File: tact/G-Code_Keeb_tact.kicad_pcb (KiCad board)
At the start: 2 copper layers, 116 x 62 mm, 28 parts, among them SW1 X+100, SW10 Y-1, SW11 Y-10, SW12 Y-100, SW13 Z+10, SW14 Z+1, SW15 Z+0.1, SW16 Z-0.1, SW17 Z-1, SW18 Z-10, SW19 HOME, SW2 X+10, SW20 HOME X, SW21 HOME Y, SW22 HOME XY, SW23 HOME Z, SW3 locked, SW5 X-10, SW6 X-100, SW7 Y+100, SW8 Y+10, SW9 Y+1, U1 Pico

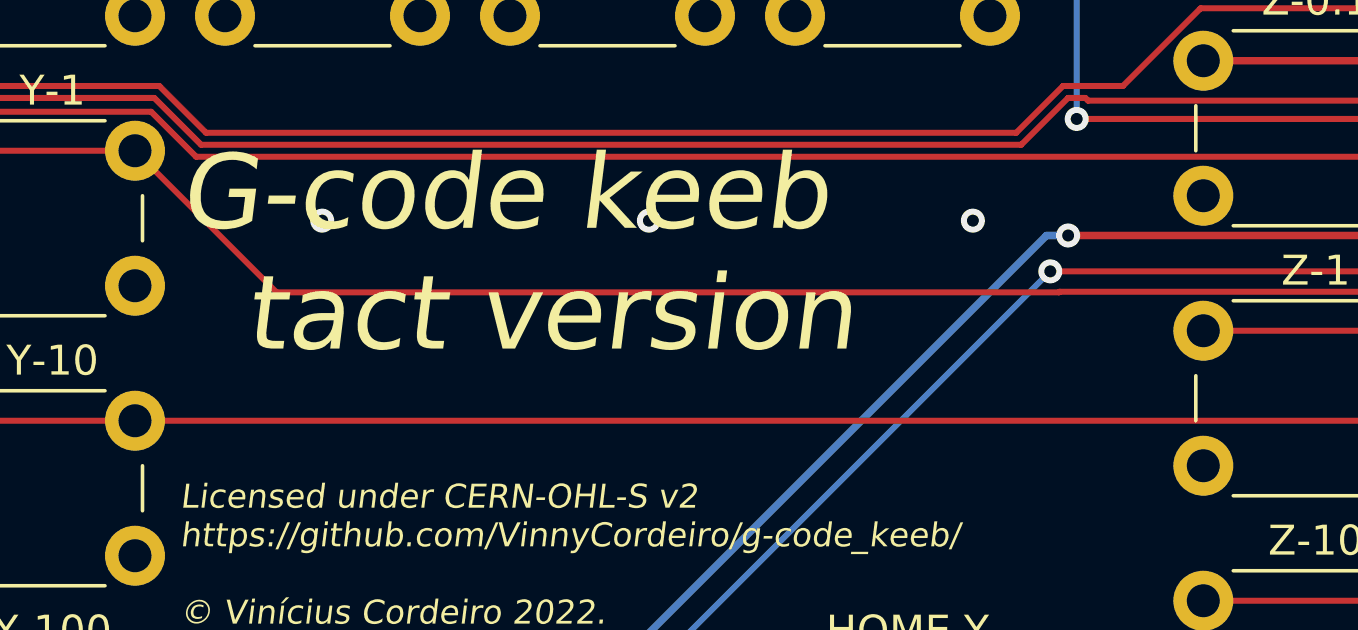
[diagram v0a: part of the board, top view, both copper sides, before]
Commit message: Adjusting silkscreen
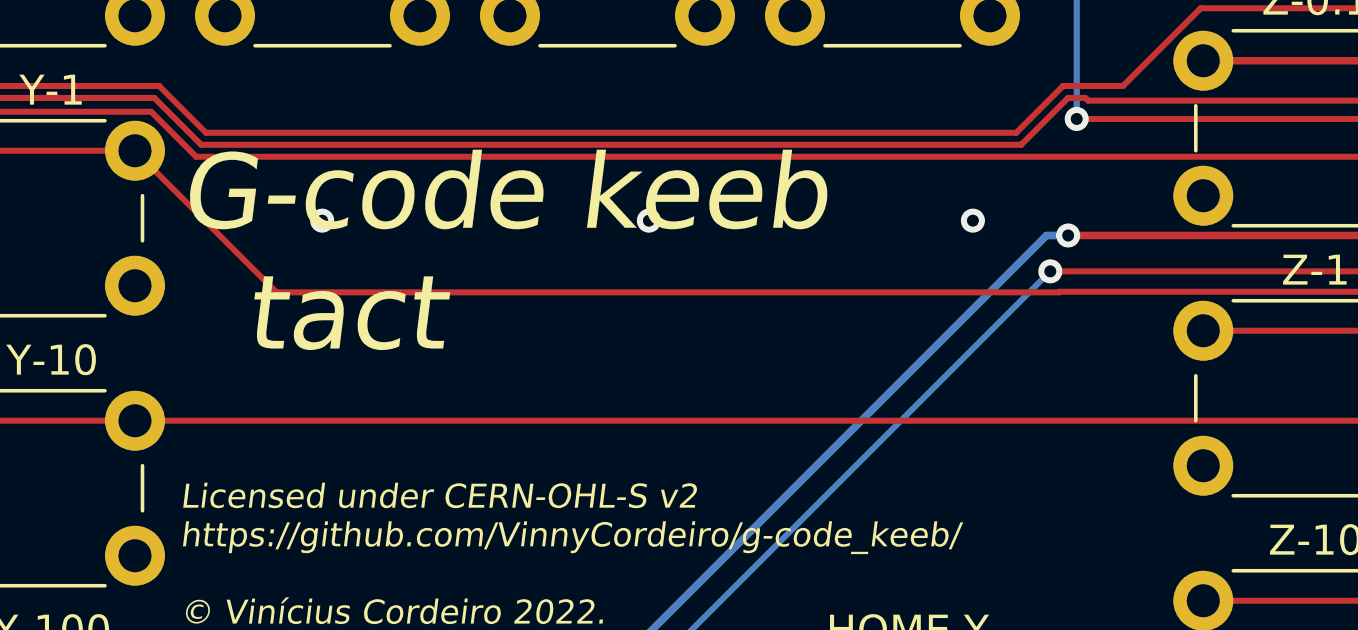
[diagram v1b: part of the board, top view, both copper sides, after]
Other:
- board text added: "G-code keeb tact"
- board text added: "HOME -> gpio19 HOME X -> gpio0 HOME Y -> gpio15 HOME XY -> gpio9 HOME Z -> gpio22"
- board text added: "X+1 -> gpio8 X+10 -> gpio7 X+100 -> gpio20 X-1 -> gpio10 X-10 -> gpio11 X-100 -> gpio12"
- board text added: "Y+1 -> gpio3 Y+10 -> gpio2 Y+100 -> gpio1 Y-1 -> gpio13 Y-10 -> gpio14 Y-100 -> gpio18"
- board text added: "Z+0.1 -> gpio26 Z+1 -> gpio27 Z+10 -> gpio28 Z-0.1 -> gpio21 Z-1 -> gpio17 Z-10 -> gpio16"
- board text removed: "G-code keeb tact version"
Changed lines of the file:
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@@
     (property "Sheetfile" "G-Code_Keeb_tact.kicad_sch")
     (property "Sheetname" "")
-    (attr through_hole)
+    (attr through_hole exclude_from_pos_files)
     (fp_text reference "U1" (at 0 0) (layer "B.SilkS")
       (effects (font (size 1 1) (thickness 0.15)) (justify mirror))
@@
     ) (layer "B.Cu") (width 0.001) (fill solid))
   (gr_rect (start 90 62) (end 206 124) (layer "Edge.Cuts") (width 0.1) (fill none))
+  (gr_text "HOME    -> gpio19\nHOME X  -> gpio0\nHOME Y  -> gpio15\nHOME XY -> gpio9\nHOME Z  -> gpio22" (at 116.53 104.54) (layer "B.SilkS")
+    (effects (font (size 1.25 1.25) (thickness 0.15)) (justify left mirror))
+  )
+  (gr_text "Z+0.1 -> gpio26\nZ+1   -> gpio27\nZ+10  -> gpio28\nZ-0.1 -> gpio21\nZ-1   -> gpio17\nZ-10  -> gpio16" (at 151.29 105.54625) (layer "B.SilkS")
+    (effects (font (size 1.25 1.25) (thickness 0.15)) (justify left mirror))
+  )
+  (gr_text "Y+1   -> gpio3\nY+10  -> gpio2\nY+100 -> gpio1\nY-1   -> gpio13\nY-10  -> gpio14\nY-100 -> gpio18" (at 116.53 77.59) (layer "B.SilkS")
+    (effects (font (size 1.25 1.25) (thickness 0.15)) (justify left mirror))
+  )
+  (gr_text "X+1   -> gpio8\nX+10  -> gpio7\nX+100 -> gpio20\nX-1   -> gpio10\nX-10  -> gpio11\nX-100 -> gpio12" (at 151.29 77.59) (layer "B.SilkS")
+    (effects (font (size 1.25 1.25) (thickness 0.15)) (justify left mirror))
+  )
   (gr_text "Licensed under CERN-OHL-S v2\nhttps://github.com/VinnyCordeiro/g-code_keeb/\n\n© Vinícius Cordeiro 2022." (at 128 113.46) (layer "F.SilkS")
     (effects (font (size 0.8 0.8) (thickness 0.15) italic) (justify left))
   )
-  (gr_text "G-code keeb\n  tact version" (at 128 103.425) (layer "F.SilkS")
+  (gr_text "G-code keeb\n  tact" (at 128 103.425) (layer "F.SilkS")
     (effects (font (size 2.5 2.5) (thickness 0.3) italic) (justify left))
   )
